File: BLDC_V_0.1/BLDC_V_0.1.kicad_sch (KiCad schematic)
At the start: 0 parts

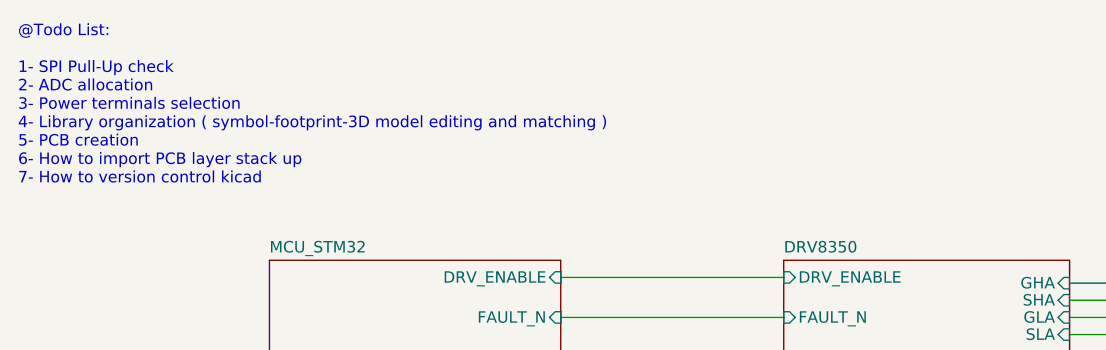
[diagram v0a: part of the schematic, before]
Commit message: Xtal changed 16MHz to 24MHz.
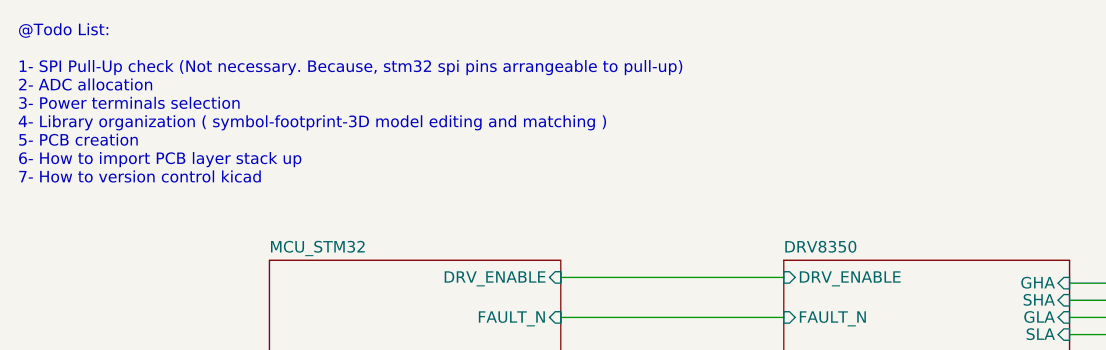
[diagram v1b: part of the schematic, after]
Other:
- note added: "@Todo List: 1- SPI Pull-Up check (Not necessary. Because, stm32 spi pins arrangeable to pull-up) 2- ADC allocation 3- Power terminals selection 4- Library organization ( symbol-footprint-3D model editing and matching ) 5- PCB creation 6- How to import PCB layer stack up 7- How to version control kicad"
- note removed: "@Todo List: 1- SPI Pull-Up check 2- ADC allocation 3- Power terminals selection 4- Library organization ( symbol-footprint-3D model editing and matching ) 5- PCB creation 6- How to import PCB layer stack up 7- How to version control kicad"
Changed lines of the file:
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@@
     (stroke (width 0) (type default))
   )
-  (text "@Todo List:\n\n1- SPI Pull-Up check\n2- ADC allocation\n3- Power terminals selection\n4- Library organization ( symbol-footprint-3D model editing and matching )\n5- PCB creation\n6- How to import PCB layer stack up\n7- How to version control kicad"
+  (text "@Todo List:\n\n1- SPI Pull-Up check (Not necessary. Because, stm32 spi pins arrangeable to pull-up)\n2- ADC allocation\n3- Power terminals selection\n4- Library organization ( symbol-footprint-3D model editing and matching )\n5- PCB creation\n6- How to import PCB layer stack up\n7- How to version control kicad"
     (at 14.605 32.385 0)
     (effects (font (size 1.27 1.27)) (justify left bottom))

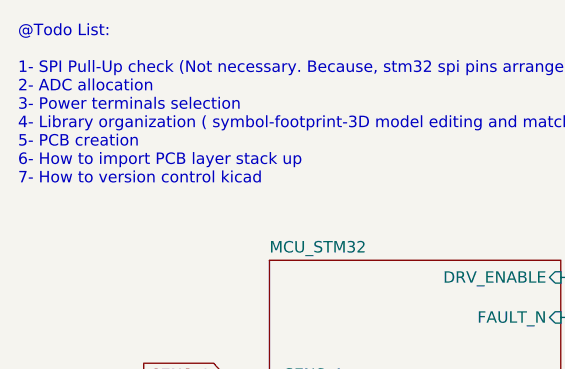
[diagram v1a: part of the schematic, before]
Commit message: MCU ADC allocation is done.
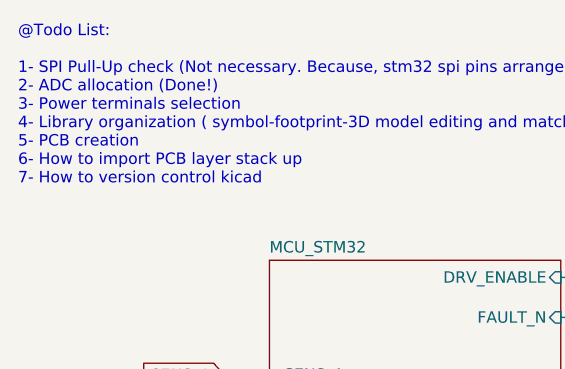
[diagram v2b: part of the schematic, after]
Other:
- note added: "@Todo List: 1- SPI Pull-Up check (Not necessary. Because, stm32 spi pins arrangeable to pull-up) 2- ADC allocation (Done!) 3- Power terminals selection 4- Library organization ( symbol-footprint-3D model editing and matching ) 5- PCB creation 6- How to import PCB layer stack up 7- How to version control kicad"
- note removed: "@Todo List: 1- SPI Pull-Up check (Not necessary. Because, stm32 spi pins arrangeable to pull-up) 2- ADC allocation 3- Power terminals selection 4- Library organization ( symbol-footprint-3D model editing and matching ) 5- PCB creation 6- How to import PCB layer stack up 7- How to version control kicad"
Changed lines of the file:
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@@
     (stroke (width 0) (type default))
   )
-  (text "@Todo List:\n\n1- SPI Pull-Up check (Not necessary. Because, stm32 spi pins arrangeable to pull-up)\n2- ADC allocation\n3- Power terminals selection\n4- Library organization ( symbol-footprint-3D model editing and matching )\n5- PCB creation\n6- How to import PCB layer stack up\n7- How to version control kicad"
+  (text "@Todo List:\n\n1- SPI Pull-Up check (Not necessary. Because, stm32 spi pins arrangeable to pull-up)\n2- ADC allocation (Done!)\n3- Power terminals selection\n4- Library organization ( symbol-footprint-3D model editing and matching )\n5- PCB creation\n6- How to import PCB layer stack up\n7- How to version control kicad"
     (at 14.605 32.385 0)
     (effects (font (size 1.27 1.27)) (justify left bottom))

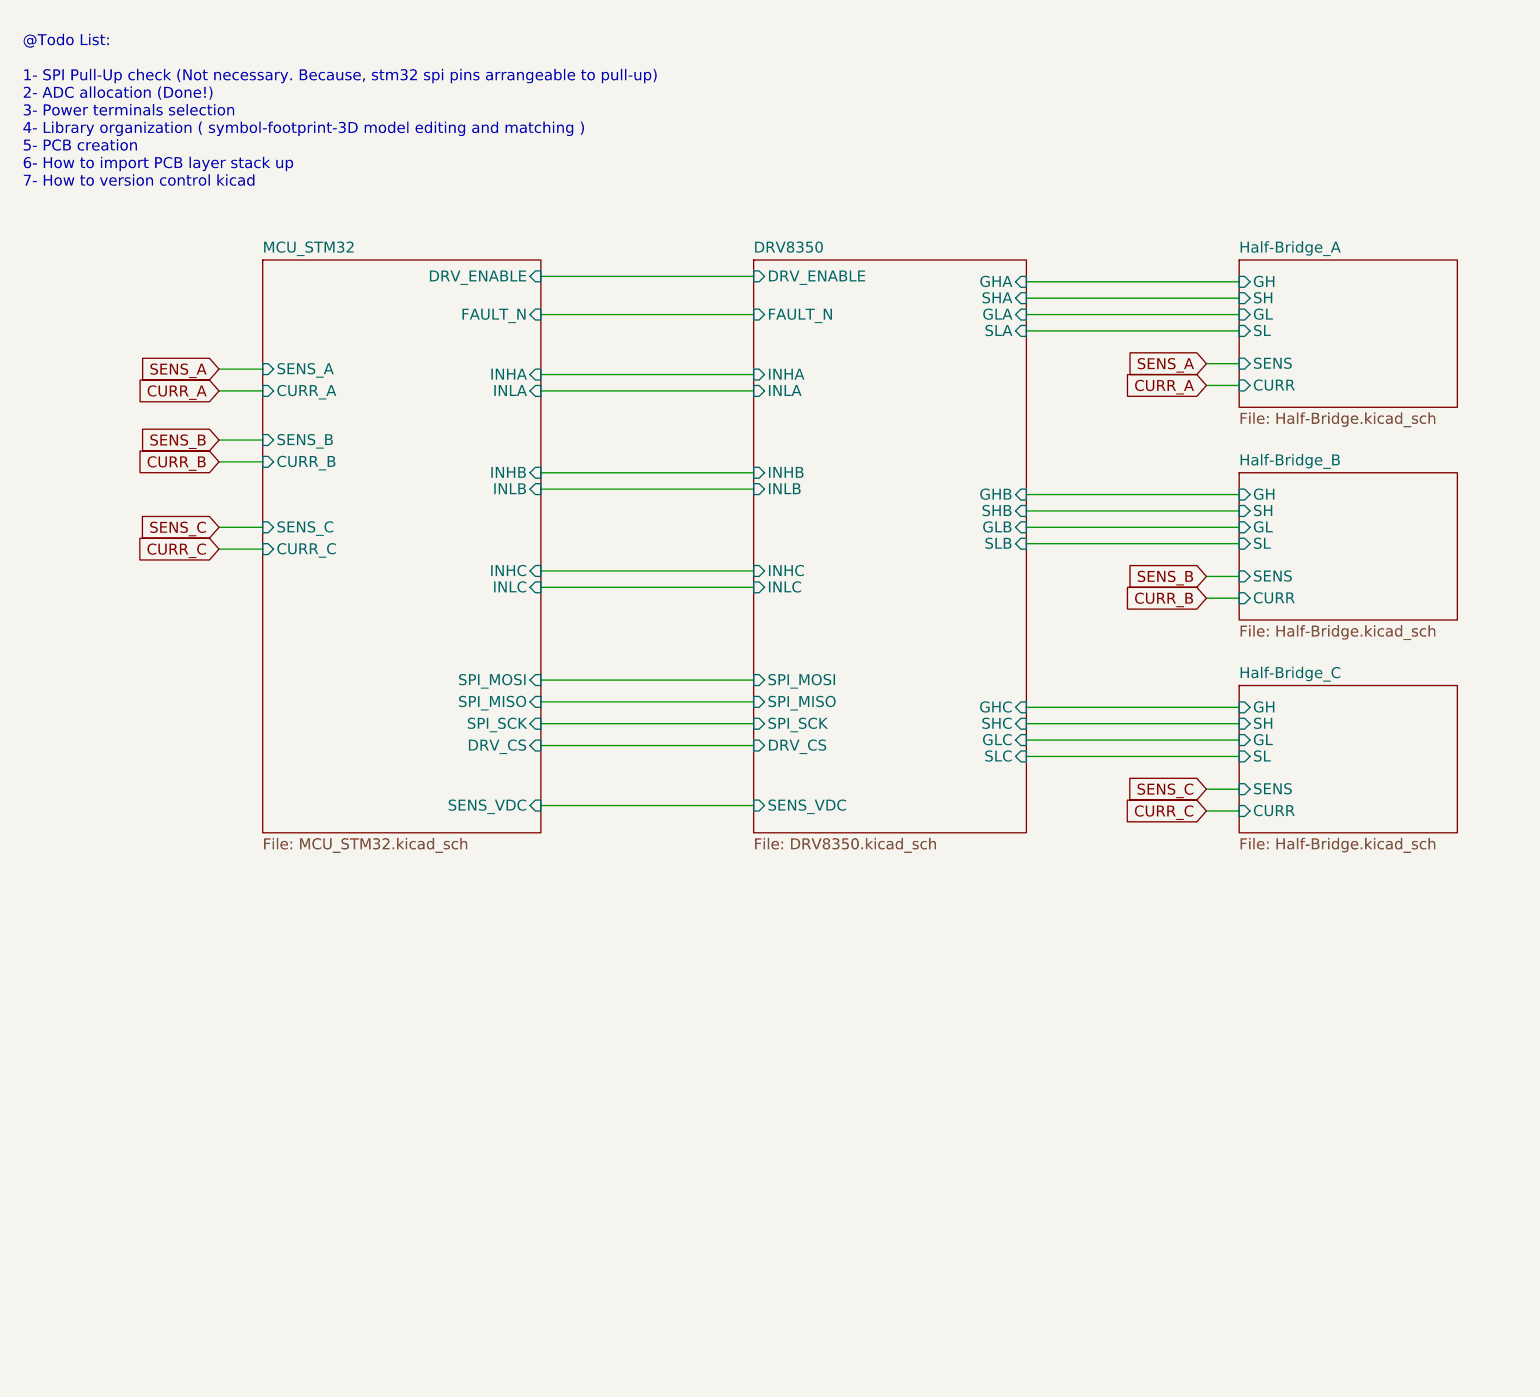
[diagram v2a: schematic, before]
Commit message: Connectors and CAN circuit added.
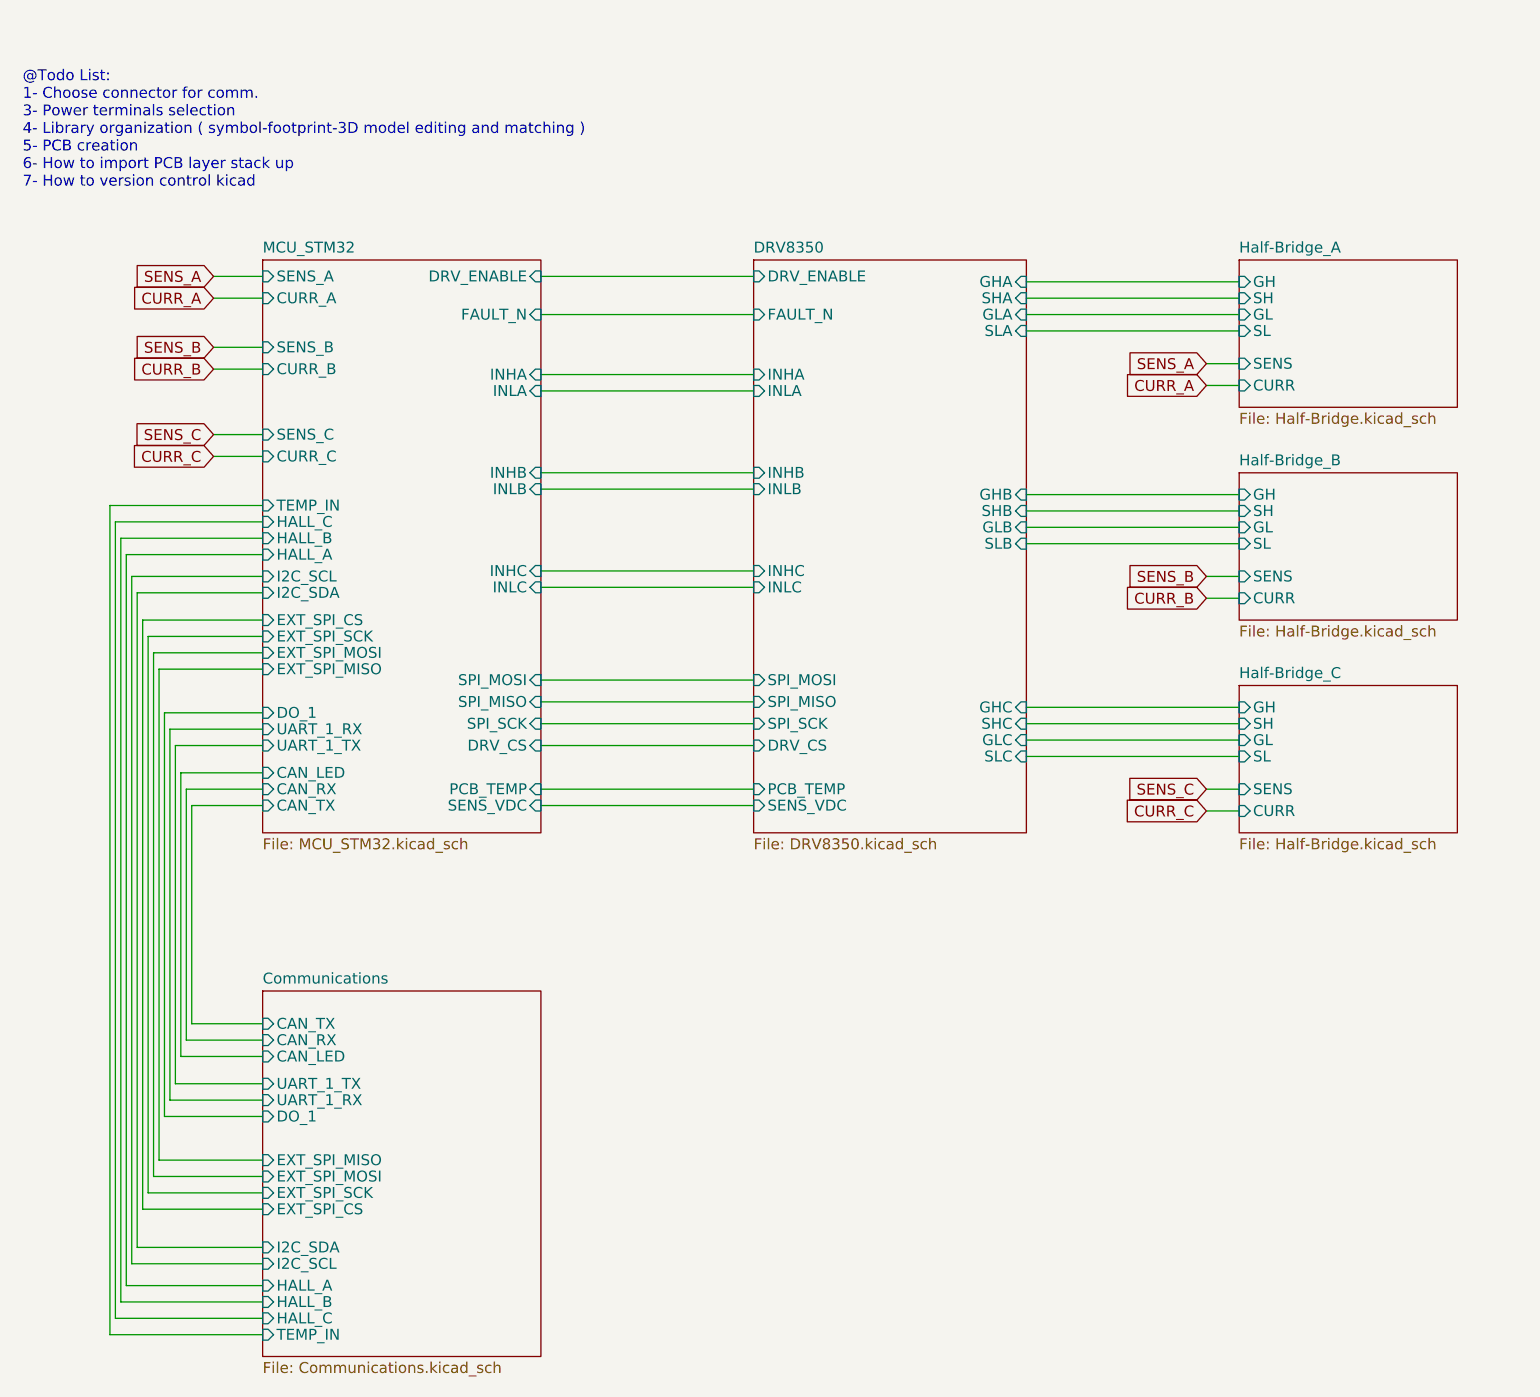
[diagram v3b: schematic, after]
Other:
- added sheet Communications (Communications.kicad_sch)
- sheet DRV8350 ports: added PCB_TEMP; removed none
- sheet MCU_STM32 ports: added CAN_LED, CAN_RX, CAN_TX, DO_1, EXT_SPI_CS, EXT_SPI_MISO, EXT_SPI_MOSI, EXT_SPI_SCK, HALL_A, HALL_B, HALL_C, I2C_SCL, I2C_SDA, PCB_TEMP, TEMP_IN, UART_1_RX, UART_1_TX; removed none
- note added: "@Todo List: 1- Choose connector for comm. 3- Power terminals selection 4- Library organization ( symbol-footprint-3D model editing and matching ) 5- PCB creation 6- How to import PCB layer stack up 7- How to version control kicad"
- note removed: "@Todo List: 1- SPI Pull-Up check (Not necessary. Because, stm32 spi pins arrangeable to pull-up) 2- ADC allocation (Done!) 3- Power terminals selection 4- Library organization ( symbol-footprint-3D model editing and matching ) 5- PCB creation 6- How to import PCB layer stack up 7- How to version control kicad"

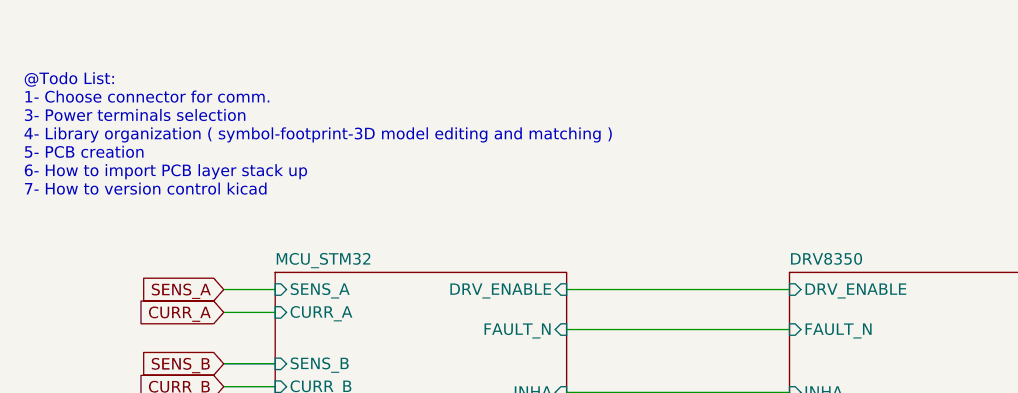
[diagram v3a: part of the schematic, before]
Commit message: Schematic prototip done.
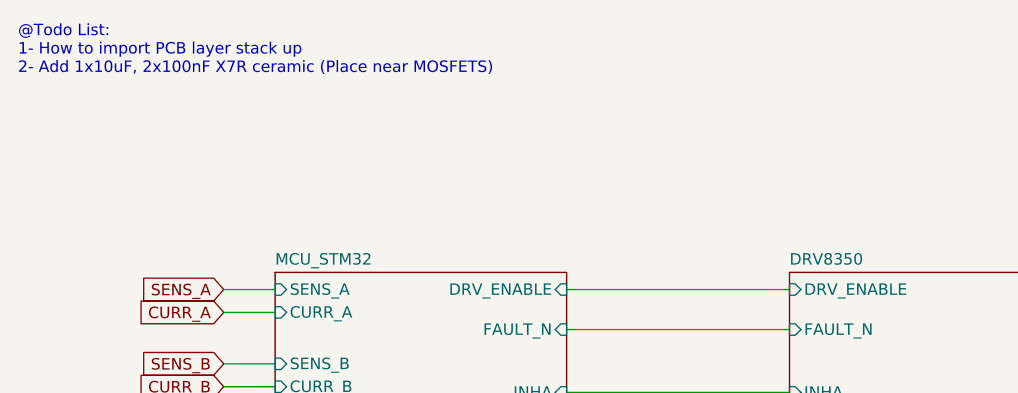
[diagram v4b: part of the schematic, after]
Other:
- note added: "@Todo List: 1- How to import PCB layer stack up 2- Add 1x10uF, 2x100nF X7R ceramic (Place near MOSFETS)"
- note removed: "@Todo List: 1- Choose connector for comm. 3- Power terminals selection 4- Library organization ( symbol-footprint-3D model editing and matching ) 5- PCB creation 6- How to import PCB layer stack up 7- How to version control kicad"
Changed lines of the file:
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@@
     (stroke (width 0) (type default))
   )
-  (text "@Todo List:\n1- Choose connector for comm.\n3- Power terminals selection\n4- Library organization ( symbol-footprint-3D model editing and matching )\n5- PCB creation\n6- How to import PCB layer stack up\n7- How to version control kicad"
-    (at 14.605 32.385 0)
+  (text "@Todo List:\n1- How to import PCB layer stack up\n2- Add 1x10uF, 2x100nF X7R ceramic (Place near MOSFETS)\n\n\n"
+    (at 13.97 22.86 0)
     (effects (font (size 1.27 1.27)) (justify left bottom))
   )

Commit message: PCB placement completed.
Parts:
- added H1, H2, H3, H4: MountingHole, MountingHole:MountingHole_3.2mm_M3, symbol Mechanical:MountingHole
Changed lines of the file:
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@@
+    )
+  )
+  (symbol (lib_id "Mechanical:MountingHole") (at 131.445 155.575 0) (unit 1)
+    (in_bom yes) (on_board yes) (dnp no) (fields_autoplaced)
+    (property "Reference" "H4" (at 134.62 154.305 0)
+      (effects (font (size 1.27 1.27)) (justify left))
+    )
+    (property "Value" "MountingHole" (at 134.62 156.845 0)
+      (effects (font (size 1.27 1.27)) (justify left))
+    )
+    (property "Footprint" "MountingHole:MountingHole_3.2mm_M3" (at 131.445 155.575 0)
+      (effects (font (size 1.27 1.27)) hide)
+    )
+    (property "Datasheet" "~" (at 131.445 155.575 0)
+      (effects (font (size 1.27 1.27)) hide)
+    )
+    (instances
+      (project "BLDC_V_0.1"
+        (path "/4cd36721-3778-4ad1-9865-468b6186ee19"
+          (reference "H4") (unit 1)
+        )
+      )
+    )
+  )
+  (symbol (lib_id "Mechanical:MountingHole") (at 131.445 139.065 0) (unit 1)
+    (in_bom yes) (on_board yes) (dnp no) (fields_autoplaced)
+    (property "Reference" "H1" (at 134.62 137.795 0)
+      (effects (font (size 1.27 1.27)) (justify left))
+    )
+    (property "Value" "MountingHole" (at 134.62 140.335 0)
+      (effects (font (size 1.27 1.27)) (justify left))
+    )
+    (property "Footprint" "MountingHole:MountingHole_3.2mm_M3" (at 131.445 139.065 0)
+      (effects (font (size 1.27 1.27)) hide)
+    )
+    (property "Datasheet" "~" (at 131.445 139.065 0)
+      (effects (font (size 1.27 1.27)) hide)
+    )
+    (instances
+      (project "BLDC_V_0.1"
+        (path "/4cd36721-3778-4ad1-9865-468b6186ee19"
+          (reference "H1") (unit 1)
+        )
+      )
+    )
+  )
+  (symbol (lib_id "Mechanical:MountingHole") (at 131.445 144.78 0) (unit 1)
+    (in_bom yes) (on_board yes) (dnp no) (fields_autoplaced)
+    (property "Reference" "H2" (at 134.62 143.51 0)
+      (effects (font (size 1.27 1.27)) (justify left))
+    )
+    (property "Value" "MountingHole" (at 134.62 146.05 0)
+      (effects (font (size 1.27 1.27)) (justify left))
+    )
+    (property "Footprint" "MountingHole:MountingHole_3.2mm_M3" (at 131.445 144.78 0)
+      (effects (font (size 1.27 1.27)) hide)
+    )
+    (property "Datasheet" "~" (at 131.445 144.78 0)
+      (effects (font (size 1.27 1.27)) hide)
+    )
+    (instances
+      (project "BLDC_V_0.1"
+        (path "/4cd36721-3778-4ad1-9865-468b6186ee19"
+          (reference "H2") (unit 1)
+        )
+      )
+    )
+  )
+  (symbol (lib_id "Mechanical:MountingHole") (at 131.445 150.495 0) (unit 1)
+    (in_bom yes) (on_board yes) (dnp no) (fields_autoplaced)
+    (property "Reference" "H3" (at 134.62 149.225 0)
+      (effects (font (size 1.27 1.27)) (justify left))
+    )
+    (property "Value" "MountingHole" (at 134.62 151.765 0)
+      (effects (font (size 1.27 1.27)) (justify left))
+    )
+    (property "Footprint" "MountingHole:MountingHole_3.2mm_M3" (at 131.445 150.495 0)
+      (effects (font (size 1.27 1.27)) hide)
+    )
+    (property "Datasheet" "~" (at 131.445 150.495 0)
+      (effects (font (size 1.27 1.27)) hide)
+    )
+    (instances
+      (project "BLDC_V_0.1"
+        (path "/4cd36721-3778-4ad1-9865-468b6186ee19"
+          (reference "H3") (unit 1)
+        )
+      )
     )
   )
